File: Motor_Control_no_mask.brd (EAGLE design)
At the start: 99.1 x 49.8 mm, 33 parts

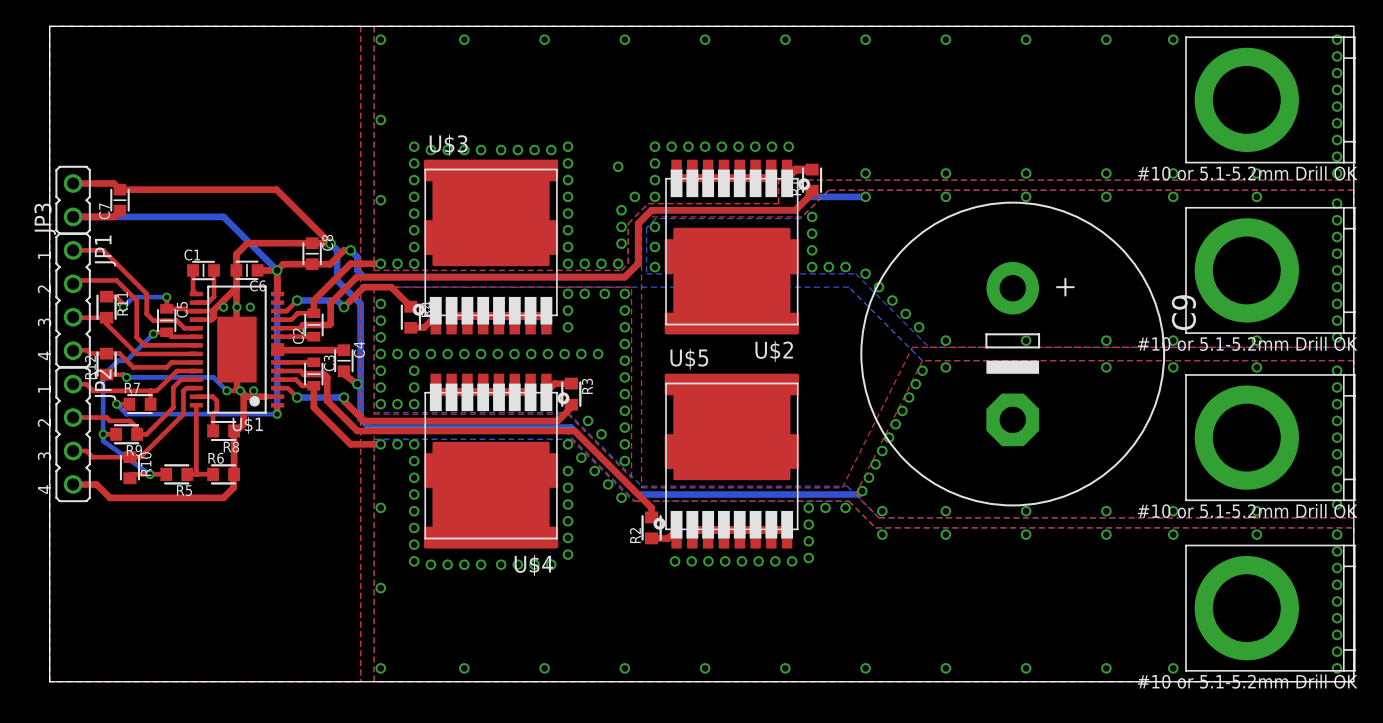
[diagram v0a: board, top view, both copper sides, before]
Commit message: Fixed the solder mask and Gate resistors
The soldermask on the bottom side has been changed so there is at least
20 mils covering the traces. this should prevent shorts.
The gate resistors are now 4.7 Ohm. I'm not 100% sure this is correct,
might change to 10 Ohm if I see issues.
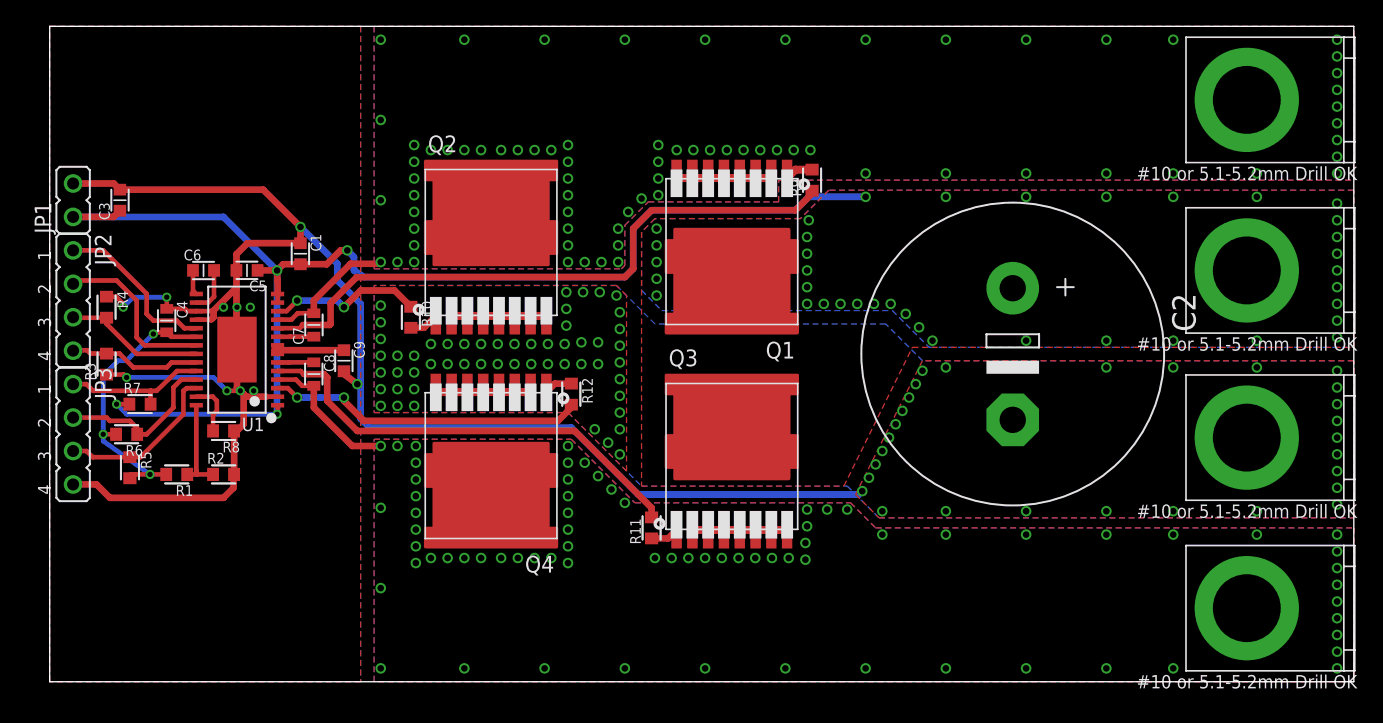
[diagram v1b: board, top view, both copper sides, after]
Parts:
- C1: value 0.47uF -> 4.7uF
- C2: value 0.22uF -> 8200uF; device Motor_Control:CAPC_0603_LONG -> Motor_Control:CAP-10-22
- C3: value 0.22uF -> 0.1uF; device Motor_Control:CAPC_0603_LONG -> Motor_Control:CAPC1608X92N
- C4: value 4.7uF -> 0.1uF; device Motor_Control:CAPC1608X92N -> Motor_Control:CAPC_0603_LONG
- C5: device Motor_Control:CAPC_0603_LONG -> Motor_Control:CAPC1608X92N
- C6: value 0.1uF -> 0.47uF
- C7: value 0.1uF -> 0.22uF; device Motor_Control:CAPC1608X92N -> Motor_Control:CAPC_0603_LONG
- C8: value 4.7uF -> 0.22uF; device Motor_Control:CAPC1608X92N -> Motor_Control:CAPC_0603_LONG
- C9: value 8200uF -> 4.7uF; device Motor_Control:CAP-10-22 -> Motor_Control:CAPC1608X92N
- JP1: device Motor_Control:JP4 -> Motor_Control:JP1
- JP3: device Motor_Control:JP1 -> Motor_Control:JP4
- R1, R3, R4: value (none) -> 10k
- R10, R11, R12, R9: value 10k -> 4.7
- R2: value (none) -> 5k
- R6: value 5k -> 10k
- moved R9 55.5 mm to (57.9, 38.1), turned to 90 degrees
- moved R1 53.2 mm to (9.65, 15.7), turned to 180 degrees
- moved C2 53.1 mm to (73.2, 24.9), turned to 270 degrees
- moved C9 50.8 mm to (22.4, 24.4)
- moved R11 44.7 mm to (45.7, 11.7), turned to 90 degrees
- moved R12 35.4 mm to (39.6, 21.8), turned to 270 degrees
- moved R3 35.4 mm to (4.32, 24.1), turned to 90 degrees
- moved R2 32.8 mm to (13.2, 15.7), turned to 0 degrees
- moved R10 24.2 mm to (27.4, 27.7)
- moved R4 23.1 mm to (4.32, 28.4)
- moved C3 19.8 mm to (5.33, 36.6), turned to 90 degrees
- moved JP3 17.8 mm to (1.78, 18.8), turned to 270 degrees
- moved C7 17.5 mm to (20.1, 27.1)
- moved C4 13.8 mm to (8.89, 27.4)
- moved JP2 10.2 mm to (1.78, 29.0)
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- renumbered U$1 to U1, U$2 to Q1, U$3 to Q2, U$4 to Q4, U$5 to Q3, U$6 to J2, U$7 to J4, U$8 to J1, U$9 to J3
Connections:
- net !RESET: now also JP3.1; no longer JP2.1
- net +VBATT: now also C1.2, C2.+, C3.1, C5.1, JP1.1; no longer C6.1, C7.1, C8.2, C9.+, JP3.1
- net FF1: now also JP3.2, R6.1; no longer JP2.2, R9.1
- net FF2: now also JP3.3, R5.1; no longer JP2.3, R10.1
- net GHA: now also R9.1; no longer R1.1
- net GHB: now also R11.2; no longer R2.2
- net GLA: now also R10.1; no longer R4.1
- net GLB: now also R12.2; no longer R3.2
- net GND: now also C1.1, C2.-, C3.2, C4.1, C5.2, C9.2, JP1.2, JP3.4, R2.2, R3.1, R4.1; no longer C4.2, C5.1, C6.2, C7.2, C8.1, C9.-, JP2.4, JP3.2, R11.1, R12.1, R6.2
- net N$1: now also R9.2; no longer R1.2
- net N$13: now also R1.1, R2.1; no longer R5.1, R6.1
- net N$15: now also C8.1; no longer C3.1
- net N$19: now also C6.1; no longer C1.1
- net N$2: now also R10.2; no longer R4.2
- net N$20: now also C6.2; no longer C1.2
- net N$3: now also R12.1; no longer R3.1
- net N$4: now also R11.1; no longer R2.1
- net N$5: now also C9.1; no longer C4.1
- net N$6: now also C7.1; no longer C2.1
- net PHASE: now also JP2.1; no longer JP1.1
- net PWMH: now also JP2.4, R3.2; no longer JP1.4, R12.2
- net PWML: now also JP2.3, R4.2; no longer JP1.3, R11.2
- net SA: now also C7.2; no longer C2.2
- net SB: now also C8.2; no longer C3.2
- net SR: now also JP2.2; no longer JP1.2
- net V5: now also C4.2, R1.2, R6.2; no longer C5.2, R10.2, R9.2
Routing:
- net GND: track 159.3 -> 157.6 mm, vias 83 -> 95
- net +VBATT: vias 38 -> 42
- net SB: track 18.0 -> 18.1 mm, vias 71 -> 73
